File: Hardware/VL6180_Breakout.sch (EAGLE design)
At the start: 23 parts, among them U1 VL6180, U3 MIC5219 3.3V

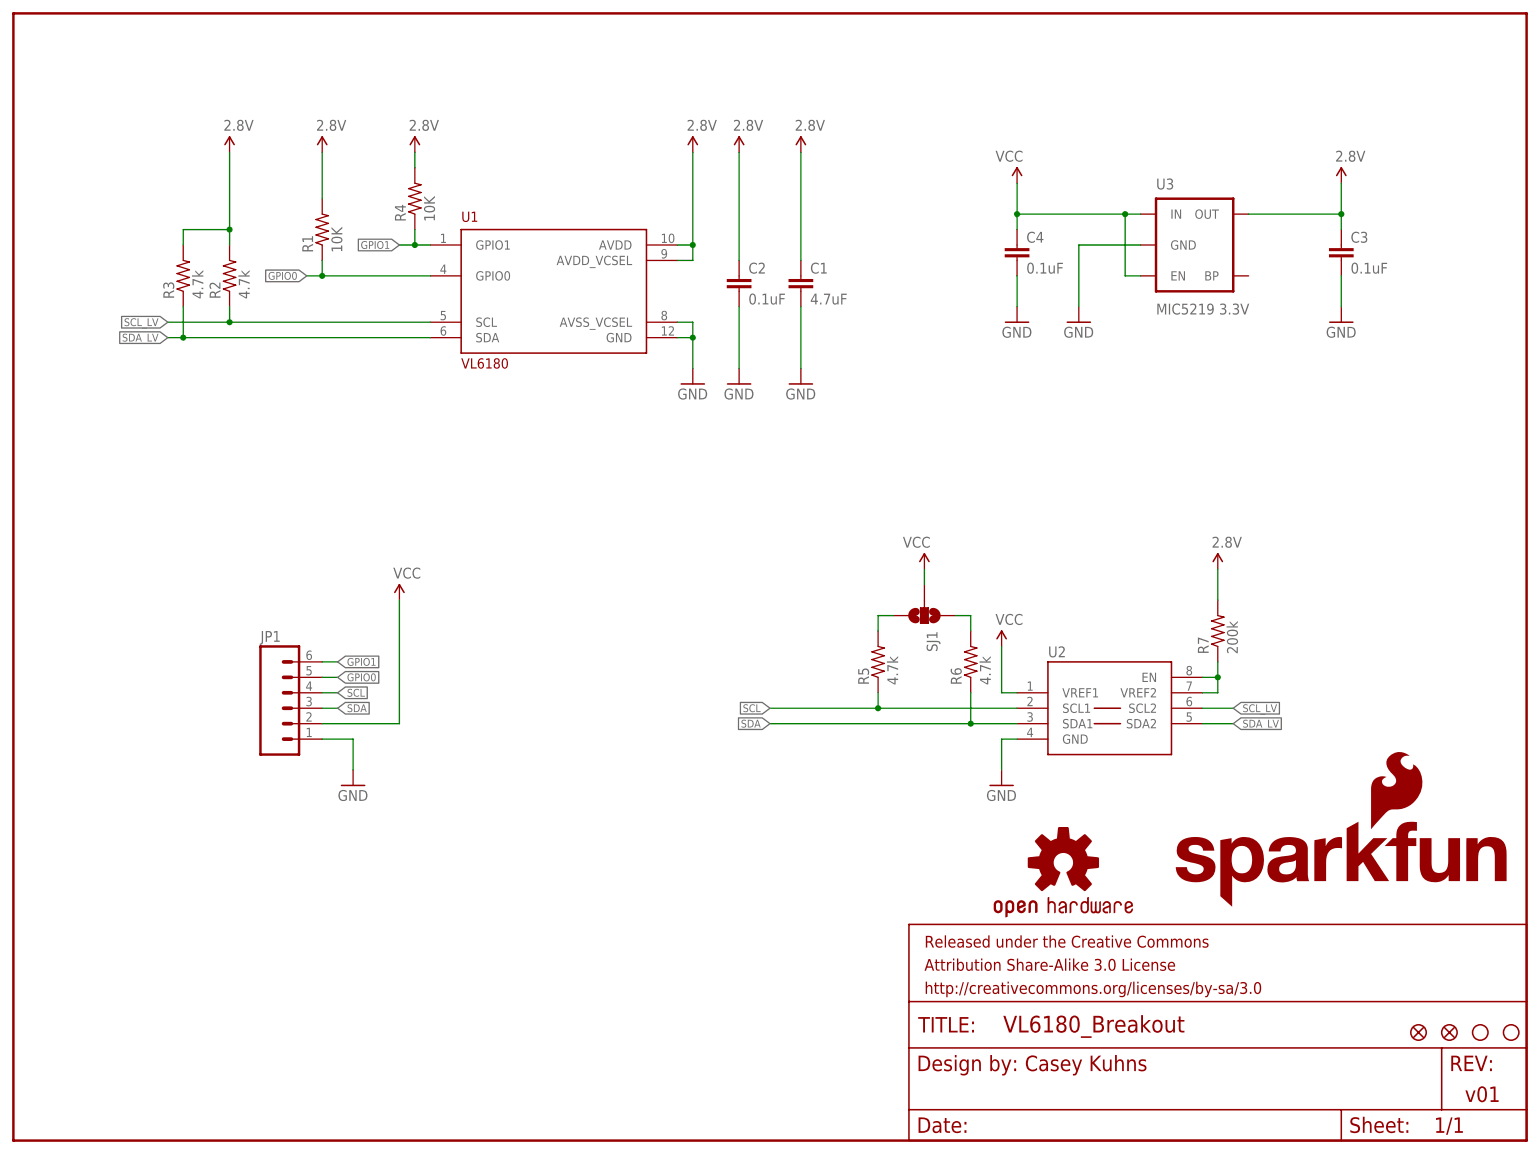
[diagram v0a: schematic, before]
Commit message: finished layout and added simple breakout board layout
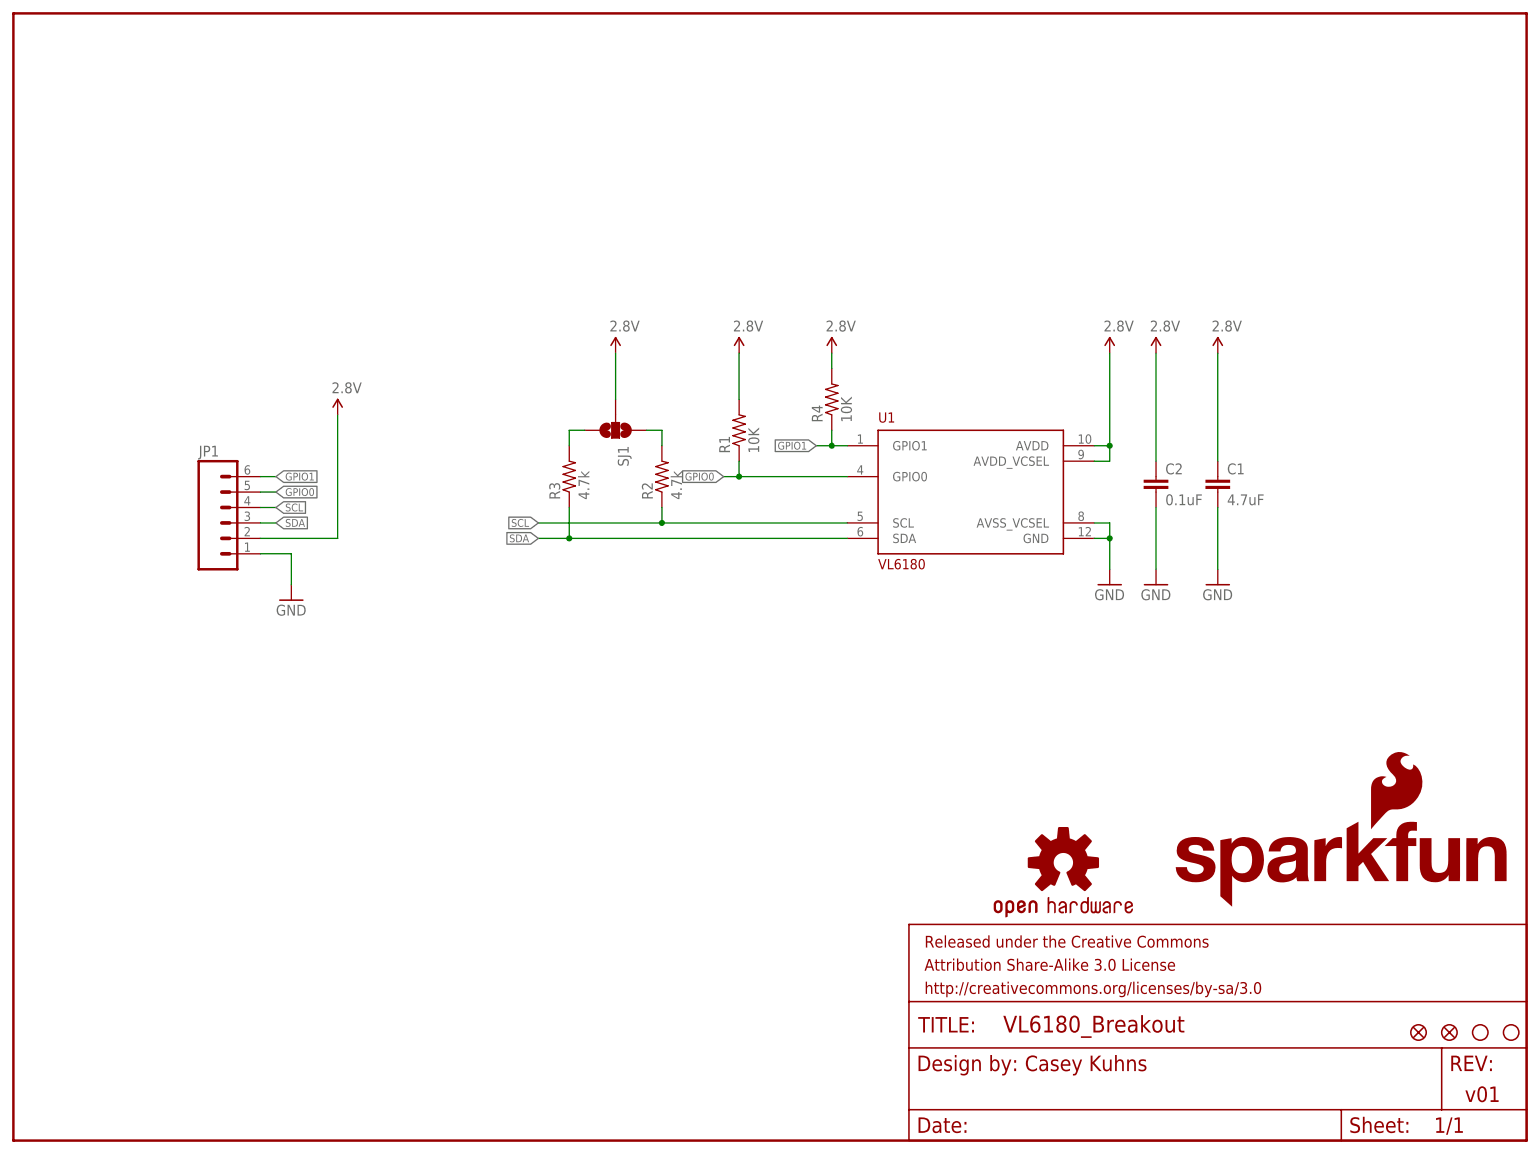
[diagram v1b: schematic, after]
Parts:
- removed C3, C4: 0.1uF, SparkFun-Capacitors:0.1UF-25V(+80/-20%)(0603)
- removed R5, R6: 4.7k, SparkFun-Resistors:4.7KOHM1/10W1%(0603)
- removed R7: 200k, SparkFun-Resistors:200KOHM1/10W1%(0603)200K
- removed U2: (no value), SparkFun-DigitalIC:PCA9306
- removed U3: MIC5219 3.3V, SparkFun-PowerIC:V_REG_MIC52193.3V
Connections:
- removed net N$3: R5.2, SJ1.3
- removed net SCL_LV: R2.1, U1.SCL, U2.SCL2
- removed net SDA_LV: R3.1, U1.SDA, U2.SDA2
- removed net VCC: C4.1, JP1.2, SJ1.2, U2.VREF1, U3.EN, U3.IN
- net 2.8V: now also JP1.2, SJ1.2; no longer C3.1, R2.2, R3.2, R7.2, U3.OUT
- net GND: no longer C3.2, C4.2, U2.GND, U3.GND
- net N$1: now also R2.2, SJ1.1; no longer R7.1, U2.EN, U2.VREF2
- net N$2: now also R3.2, SJ1.3; no longer R6.2, SJ1.1
- net SCL: now also R2.1, U1.SCL; no longer R5.1, U2.SCL1
- net SDA: now also R3.1, U1.SDA; no longer R6.1, U2.SDA1
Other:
- moved on the sheet: C1, C2, JP1, R1, R2, R3, R4, SJ1, U1

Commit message: added pin 1 designator
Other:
- note added: "v03"
- note removed: "v01"
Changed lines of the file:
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@@
 <plain>
 <text x="166.37" y="11.43" size="2.54" layer="94">Casey Kuhns</text>
-<text x="238.76" y="6.35" size="2.54" layer="94">v01</text>
+<text x="238.76" y="6.35" size="2.54" layer="94">v03</text>
 </plain>
 <instances>

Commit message: modified:   Hardware/VL6180_Breakout.brd 	modified:   Hardware/VL6180_Breakout.sch 	renamed:    Hardware/VL6180.brd -> Hardware/VL6180_Sensor.brd 	renamed:    Hardware/VL6180.sch -> Hardware/VL6180_Sensor.sch
Removed I2C level shifter and switched to Fet bases solution.
New solderpaste footprint for VL6180 for improved reflow.
updated all parts with Sparkle ID's
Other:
- note added: "v04"
- note removed: "v03"
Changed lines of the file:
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@@
 <plain>
 <text x="166.37" y="11.43" size="2.54" layer="94">Casey Kuhns</text>
-<text x="238.76" y="6.35" size="2.54" layer="94">v03</text>
+<text x="238.76" y="6.35" size="2.54" layer="94">v04</text>
 </plain>
 <instances>

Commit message: changed I2C resistors to 2.2k, added current limiting resistor on GPIO pins.
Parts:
- R1, R4: value 10K -> 47K; device SparkFun-Resistors:10KOHM1/10W1%(0603)0603 -> SparkFun-Resistors:47KOHM1/10W1%(0603)
- R2, R3: value 4.7k -> 2.2k; device SparkFun-Resistors:4.7KOHM1/10W1%(0603) -> SparkFun-Resistors:2.2KOHM1/10W1%(0603)
- SJ1: value (none) -> JUMPER-PAD-3-NC_BY_PASTE; device SparkFun-Passives:SOLDERJUMPER_2WAYPASTE1&2&3 -> SparkFun-Passives:JUMPER-PAD-3-NC_BY_PASTE
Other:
- note added: "Default Address: 0x29"
- note added: "NOTE: This part is 1.8v - 2.8v tolerant"
- note added: "v10"
- note removed: "v04"
- moved on the sheet: R2, R3
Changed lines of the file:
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@@
 <layer number="54" name="bGND_GNDA" color="1" fill="9" visible="no" active="no"/>
 <layer number="56" name="wert" color="7" fill="1" visible="no" active="no"/>
+<layer number="57" name="tCAD" color="7" fill="1" visible="no" active="no"/>
 <layer number="91" name="Nets" color="2" fill="1" visible="yes" active="yes"/>
 <layer number="92" name="Busses" color="1" fill="1" visible="yes" active="yes"/>
@@
 <layer number="97" name="Info" color="7" fill="1" visible="yes" active="yes"/>
 <layer number="98" name="Guide" color="6" fill="1" visible="yes" active="yes"/>
+<layer number="99" name="SpiceOrder" color="7" fill="1" visible="yes" active="yes"/>
 <layer number="100" name="Muster" color="7" fill="1" visible="no" active="no"/>
 <layer number="101" name="Patch_Top" color="12" fill="4" visible="yes" active="yes"/>
@@
 <layer number="108" name="tplace-old" color="10" fill="1" visible="yes" active="yes"/>
 <layer number="109" name="ref-old" color="11" fill="1" visible="yes" active="yes"/>
+<layer number="110" name="fp0" color="7" fill="1" visible="yes" active="yes"/>
+<layer number="111" name="LPC17xx" color="7" fill="1" visible="yes" active="yes"/>
+<layer number="112" name="tSilk" color="7" fill="1" visible="yes" active="yes"/>
+<layer number="113" name="IDFDebug" color="4" fill="1" visible="yes" active="yes"/>
 <layer number="116" name="Patch_BOT" color="9" fill="4" visible="yes" active="yes"/>
 <layer number="121" name="_tsilk" color="7" fill="1" visible="yes" active="yes"/>
 <layer number="122" name="_bsilk" color="7" fill="1" visible="yes" active="yes"/>
+<layer number="123" name="tTestmark" color="7" fill="1" visible="yes" active="yes"/>
+<layer number="124" name="bTestmark" color="7" fill="1" visible="yes" active="yes"/>
 <layer number="125" name="_tNames" color="7" fill="1" visible="yes" active="yes"/>
+<layer number="126" name="_bNames" color="7" fill="1" visible="yes" active="yes"/>
+<layer number="127" name="_tValues" color="7" fill="1" visible="yes" active="yes"/>
+<layer number="128" name="_bValues" color="7" fill="1" visible="yes" active="yes"/>
+<layer number="131" name="tAdjust" color="7" fill="1" visible="yes" active="yes"/>
+<layer number="132" name="bAdjust" color="7" fill="1" visible="yes" active="yes"/>
 <layer number="144" name="Drill_legend" color="7" fill="1" visible="yes" active="yes"/>
+<layer number="150" name="Notes" color="7" fill="1" visible="yes" active="yes"/>
 <layer number="151" name="HeatSink" color="7" fill="1" visible="yes" active="yes"/>
+<layer number="152" name="_bDocu" color="7" fill="1" visible="yes" active="yes"/>
+<layer number="153" name="FabDoc1" color="7" fill="1" visible="yes" active="yes"/>
+<layer number="154" name="FabDoc2" color="7" fill="1" visible="yes" active="yes"/>
+<layer number="155" name="FabDoc3" color="7" fill="1" visible="yes" active="yes"/>
 <layer number="199" name="Contour" color="7" fill="1" visible="yes" active="yes"/>
 <layer number="200" name="200bmp" color="1" fill="10" visible="yes" active="yes"/>
@@
 <layer number="223" name="223bmp" color="24" fill="1" visible="no" active="no"/>
 <layer number="224" name="224bmp" color="25" fill="1" visible="no" active="no"/>
+<layer number="248" name="Housing" color="7" fill="1" visible="yes" active="yes"/>
+<layer number="249" name="Edge" color="7" fill="1" visible="yes" active="yes"/>
 <layer number="250" name="Descript" color="3" fill="1" visible="no" active="no"/>
 <layer number="251" name="SMDround" color="12" fill="11" visible="no" active="no"/>
@@
 <part name="FRAME1" library="SparkFun-Aesthetics" deviceset="FRAME-LETTER" device=""/>
 <part name="U1" library="VL6180" deviceset="VL6180" device=""/>
-<part name="R2" library="SparkFun-Resistors" deviceset="4.7KOHM1/10W1%(0603)" device="" value="4.7k"/>
-<part name="R3" library="SparkFun-Resistors" deviceset="4.7KOHM1/10W1%(0603)" device="" value="4.7k"/>
-<part name="R4" library="SparkFun-Resistors" deviceset="10KOHM1/10W1%(0603)" device="0603" value="10K"/>
+<part name="R2" library="SparkFun-Resistors" deviceset="2.2KOHM1/10W1%(0603)" device="" value="2.2k"/>
+<part name="R3" library="SparkFun-Resistors" deviceset="2.2KOHM1/10W1%(0603)" device="" value="2.2k"/>
+<part name="R4" library="SparkFun-Resistors" deviceset="47KOHM1/10W1%(0603)" device="" value="47K"/>
 <part name="C1" library="SparkFun-Capacitors" deviceset="4.7UF-6.3V-10%(0603)" device="0603" value="4.7uF"/>
 <part name="C2" library="SparkFun-Capacitors" deviceset="0.1UF-25V(+80/-20%)(0603)" device="" value="0.1uF"/>
@@
 <part name="SUPPLY8" library="SparkFun-Aesthetics" deviceset="2.8V" device=""/>
 <part name="SUPPLY9" library="SparkFun-Aesthetics" deviceset="2.8V" device=""/>
-<part name="R1" library="SparkFun-Resistors" deviceset="10KOHM1/10W1%(0603)" device="0603" value="10K"/>
+<part name="R1" library="SparkFun-Resistors" deviceset="47KOHM1/10W1%(0603)" device="" value="47K"/>
 <part name="LOGO1" library="SparkFun-Aesthetics" deviceset="SFE_LOGO_NAME_FLAME" device=".1_INCH"/>
 <part name="LOGO2" library="SparkFun-Aesthetics" deviceset="OSHW-LOGO" device="S"/>
@@
 <part name="FID2" library="SparkFun-Aesthetics" deviceset="FIDUCIAL" device="1X2"/>
 <part name="SUPPLY4" library="SparkFun-Aesthetics" deviceset="2.8V" device=""/>
-<part name="SJ1" library="SparkFun-Passives" deviceset="SOLDERJUMPER_2WAY" device="PASTE1&amp;2&amp;3"/>
+<part name="SJ1" library="SparkFun-Passives" deviceset="JUMPER-PAD-3-NC_BY_PASTE" device="" value=""/>
 </parts>
 <sheets>
@@
 <plain>
 <text x="166.37" y="11.43" size="2.54" layer="94">Casey Kuhns</text>
-<text x="238.76" y="6.35" size="2.54" layer="94">v04</text>
+<text x="238.76" y="6.35" size="2.54" layer="94">v10</text>
+<text x="142.24" y="88.9" size="1.778" layer="94">Default Address: 0x29</text>
+<text x="142.24" y="81.28" size="1.778" layer="94">NOTE: This part is 1.8v - 2.8v tolerant</text>
 </plain>
 <instances>
@@
 <instance part="FRAME1" gate="G$2" x="147.32" y="0"/>
 <instance part="U1" gate="G$1" x="157.48" y="106.68"/>
-<instance part="R2" gate="G$1" x="106.68" y="109.22" rot="R90"/>
-<instance part="R3" gate="G$1" x="91.44" y="109.22" rot="R90"/>
+<instance part="R2" gate="G$1" x="104.14" y="109.22" rot="R90"/>
+<instance part="R3" gate="G$1" x="88.9" y="109.22" rot="R90"/>
 <instance part="R4" gate="G$1" x="134.62" y="121.92" rot="R90"/>
 <instance part="C1" gate="G$1" x="198.12" y="106.68"/>
@@
 <instance part="SUPPLY7" gate="G$1" x="134.62" y="129.54"/>
 <instance part="SUPPLY8" gate="G$1" x="119.38" y="129.54"/>
-<instance part="SUPPLY9" gate="G$1" x="99.06" y="129.54"/>
+<instance part="SUPPLY9" gate="G$1" x="96.52" y="129.54"/>
 <instance part="R1" gate="G$1" x="119.38" y="116.84" rot="R90"/>
 <instance part="LOGO1" gate="G$1" x="190.5" y="38.1"/>
@@
 <instance part="FID2" gate="G$1" x="231.14" y="17.78"/>
 <instance part="SUPPLY4" gate="G$1" x="53.34" y="119.38"/>
-<instance part="SJ1" gate="G$1" x="99.06" y="116.84" rot="R270"/>
+<instance part="SJ1" gate="G$1" x="96.52" y="116.84" rot="R270"/>
 </instances>
 <busses>
@@
 <segment>
 <pinref part="U1" gate="G$1" pin="SCL"/>
-<wire x1="137.16" y1="101.6" x2="106.68" y2="101.6" width="0.1524" layer="91"/>
+<wire x1="137.16" y1="101.6" x2="104.14" y2="101.6" width="0.1524" layer="91"/>
 <pinref part="R2" gate="G$1" pin="1"/>
-<wire x1="106.68" y1="104.14" x2="106.68" y2="101.6" width="0.1524" layer="91"/>
-<junction x="106.68" y="101.6"/>
-<wire x1="106.68" y1="101.6" x2="86.36" y2="101.6" width="0.1524" layer="91"/>
-<label x="86.36" y="101.6" size="1.27" layer="95" rot="R180" xref="yes"/>
+<wire x1="104.14" y1="104.14" x2="104.14" y2="101.6" width="0.1524" layer="91"/>
+<junction x="104.14" y="101.6"/>
+<wire x1="104.14" y1="101.6" x2="83.82" y2="101.6" width="0.1524" layer="91"/>
+<label x="83.82" y="101.6" size="1.27" layer="95" rot="R180" xref="yes"/>
 </segment>
 </net>
@@
 <segment>
 <pinref part="U1" gate="G$1" pin="SDA"/>
-<wire x1="137.16" y1="99.06" x2="91.44" y2="99.06" width="0.1524" layer="91"/>
+<wire x1="137.16" y1="99.06" x2="88.9" y2="99.06" width="0.1524" layer="91"/>
 <pinref part="R3" gate="G$1" pin="1"/>
-<wire x1="91.44" y1="99.06" x2="91.44" y2="104.14" width="0.1524" layer="91"/>
-<wire x1="91.44" y1="99.06" x2="86.36" y2="99.06" width="0.1524" layer="91"/>
-<junction x="91.44" y="99.06"/>
-<label x="86.36" y="99.06" size="1.27" layer="95" rot="R180" xref="yes"/>
+<wire x1="88.9" y1="99.06" x2="88.9" y2="104.14" width="0.1524" layer="91"/>
+<wire x1="88.9" y1="99.06" x2="83.82" y2="99.06" width="0.1524" layer="91"/>
+<junction x="88.9" y="99.06"/>
+<label x="83.82" y="99.06" size="1.27" layer="95" rot="R180" xref="yes"/>
 </segment>
 </net>
@@
 <pinref part="SJ1" gate="G$1" pin="2"/>
 <pinref part="SUPPLY9" gate="G$1" pin="2.8V"/>
-<wire x1="99.06" y1="129.54" x2="99.06" y2="121.92" width="0.1524" layer="91"/>
+<wire x1="96.52" y1="129.54" x2="96.52" y2="121.92" width="0.1524" layer="91"/>
 </segment>
 </net>
@@
 <pinref part="R2" gate="G$1" pin="2"/>
 <pinref part="SJ1" gate="G$1" pin="1"/>
-<wire x1="106.68" y1="114.3" x2="106.68" y2="116.84" width="0.1524" layer="91"/>
-<wire x1="106.68" y1="116.84" x2="104.14" y2="116.84" width="0.1524" layer="91"/>
+<wire x1="104.14" y1="114.3" x2="104.14" y2="116.84" width="0.1524" layer="91"/>
+<wire x1="104.14" y1="116.84" x2="101.6" y2="116.84" width="0.1524" layer="91"/>
 </segment>
 </net>
@@
 <segment>
 <pinref part="R3" gate="G$1" pin="2"/>
-<wire x1="91.44" y1="114.3" x2="91.44" y2="116.84" width="0.1524" layer="91"/>
+<wire x1="88.9" y1="114.3" x2="88.9" y2="116.84" width="0.1524" layer="91"/>
 <pinref part="SJ1" gate="G$1" pin="3"/>
-<wire x1="91.44" y1="116.84" x2="93.98" y2="116.84" width="0.1524" layer="91"/>
-</segment>
-</net>
+<wire x1="88.9" y1="116.84" x2="91.44" y2="116.84" width="0.1524" layer="91"/>
+</segment>
+</net>
